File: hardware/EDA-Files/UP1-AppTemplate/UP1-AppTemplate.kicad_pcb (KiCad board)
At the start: 2 copper layers, 39 x 21.4 mm, 1 part, among them J1 OpenKNX_UP1-Controller2040

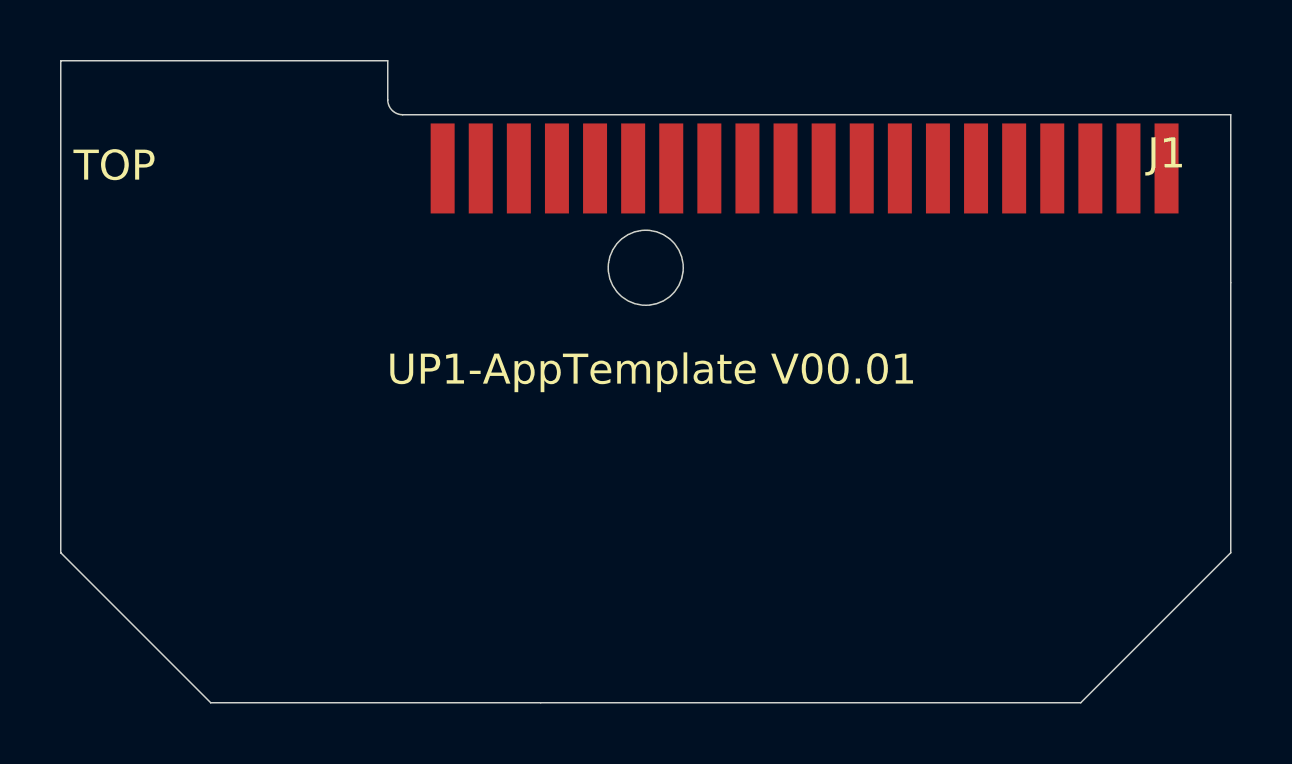
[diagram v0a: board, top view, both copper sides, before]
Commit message: reduced the spacer to the controller 0.3mm
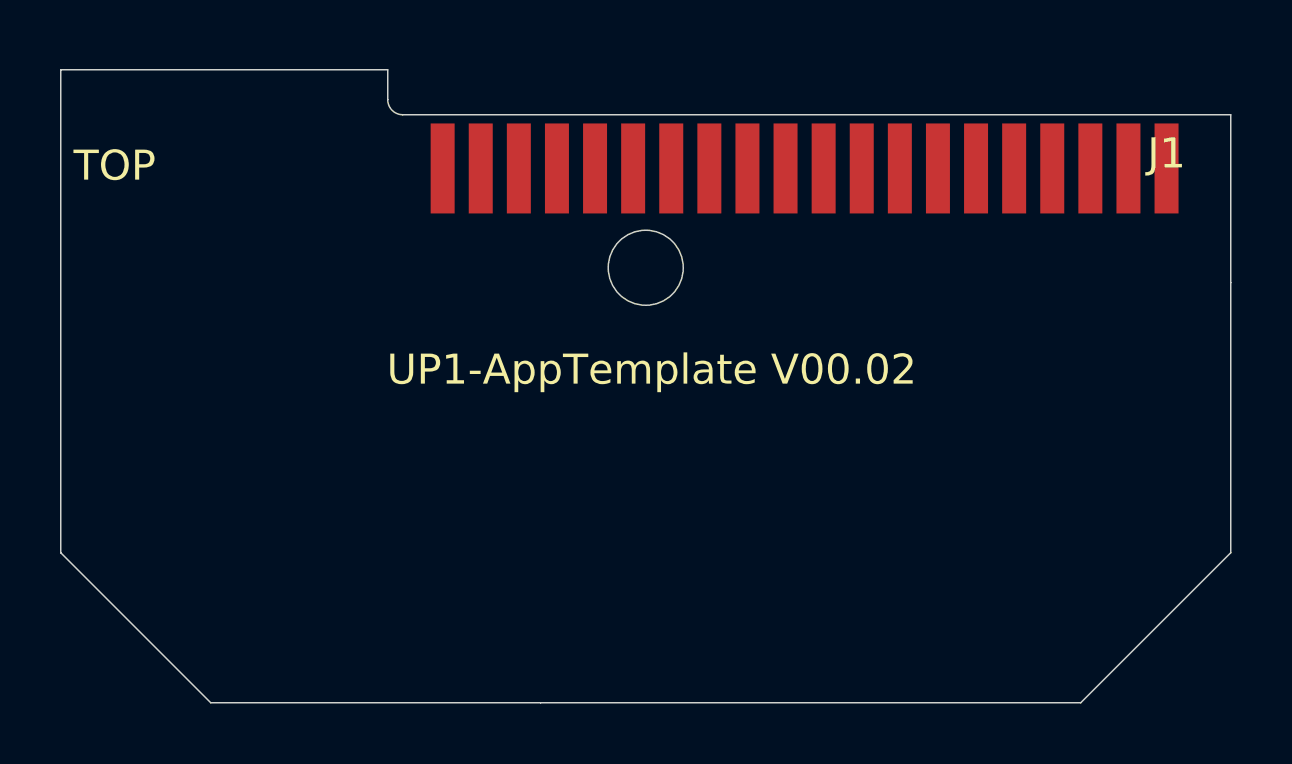
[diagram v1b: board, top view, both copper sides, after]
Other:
- board size 39 x 21.4 mm -> 39 x 21.1 mm
- board text added: "UP1-AppTemplate V00.02"
- board text removed: "UP1-AppTemplate V00.01"
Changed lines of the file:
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@@
   (page A4)
   (title_block
-    (date 2022-02-11)
-    (rev V00.01)
+    (date 2022-03-08)
+    (rev V00.02)
   )
   (layers
@@
   (gr_line (start 129 120.4) (end 129 126) (layer Edge.Cuts) (width 0.05))
   (gr_arc (start 101.4 119.9) (end 100.9 119.9) (angle -90) (layer Edge.Cuts) (width 0.05))
-  (gr_line (start 100.9 118.6) (end 100.9 119.9) (layer Edge.Cuts) (width 0.05))
+  (gr_line (start 100.9 118.9) (end 100.9 119.9) (layer Edge.Cuts) (width 0.05))
   (gr_line (start 129 135) (end 124 140) (layer Edge.Cuts) (width 0.05))
   (gr_line (start 129 120.4) (end 101.4 120.4) (layer Edge.Cuts) (width 0.05))
-  (gr_line (start 90 118.6) (end 90 135) (layer Edge.Cuts) (width 0.05))
+  (gr_line (start 90 118.9) (end 90 135) (layer Edge.Cuts) (width 0.05))
   (gr_line (start 129 126) (end 129 135) (layer Edge.Cuts) (width 0.05))
   (gr_line (start 95 140) (end 90 135) (layer Edge.Cuts) (width 0.05))
@@
     (arrow2b (pts (xy 87 101) (xy 87.586421 102.126504)))
   )
-  (gr_line (start 90 118.6) (end 100.9 118.6) (layer Edge.Cuts) (width 0.05))
+  (gr_line (start 90 118.9) (end 100.9 118.9) (layer Edge.Cuts) (width 0.05))
   (gr_circle (center 109.5 125.5) (end 109.5 124.25) (layer Edge.Cuts) (width 0.05))
   (gr_line (start 124 101) (end 95 101) (layer Eco2.User) (width 0.15))
   (gr_line (start 129 118.6) (end 90 118.6) (layer Eco2.User) (width 0.15))
   (gr_line (start 90 106) (end 95 101) (layer Eco2.User) (width 0.15))
-  (gr_text "UP1-AppTemplate V00.01" (at 109.7 128.9) (layer F.SilkS)
+  (gr_text "UP1-AppTemplate V00.02" (at 109.7 128.9) (layer F.SilkS)
     (effects (font (size 1 1) (thickness 0.15)))
   )
@@
   )
   (gr_line (start 109.5 142.5) (end 109.5 97.5) (layer Eco1.User) (width 0.15))
-  (gr_text "UP1-AppTemplate V00.01" (at 109.6 128.9) (layer B.SilkS)
+  (gr_text "UP1-AppTemplate V00.02" (at 109.6 128.9) (layer B.SilkS)
     (effects (font (size 1 1) (thickness 0.15)) (justify mirror))
   )
